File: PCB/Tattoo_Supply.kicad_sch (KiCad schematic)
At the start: 6 parts, among them J1 Barrel_Jack_Switch, J2 Out_{1}, J3 Out_{2}, Q1 SiA441DJ

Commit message: continue bom
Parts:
- J2, J3: footprint (none) -> TattooSupplyFootprints:MJ63022A
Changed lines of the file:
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@@
     (rev "V1.0")
   )
-  (bus_alias "USB2" (members "D+" "D-"))
-  (bus_alias "SPI" (members "~{CS}" "SCK" "MOSI" "MISO"))
-  (bus_alias "Encoder" (members "DT" "CLK" "SW"))
   (bus_alias "UART" (members "Tx" "Rx"))
   (bus_alias "I2C" (members "SDA" "SCL"))
+  (bus_alias "SPI" (members "~{CS}" "SCK" "MOSI" "MISO"))
+  (bus_alias "USB2" (members "D+" "D-"))
+  (bus_alias "Encoder" (members "DT" "CLK" "SW"))
   (junction (at 46.99 119.38) (diameter 0) (color 0 0 0 0)
   )
@@
       (effects (font (size 1.27 1.27)) (justify right))
     )
-    (property "Footprint" "" (at 251.46 43.18 0)
+    (property "Footprint" "TattooSupplyFootprints:MJ63022A" (at 251.46 43.18 0)
       (effects (font (size 1.27 1.27)) hide)
     )
@@
       (effects (font (size 1.27 1.27)) (justify right))
     )
-    (property "Footprint" "" (at 251.46 74.93 0)
-      (effects (font (size 1.27 1.27)) hide)
-    )
+    (property "Footprint" "TattooSupplyFootprints:MJ63022A" (at 251.46 74.93 0)
+      (effects (font (size 1.27 1.27)) hide)
+    )

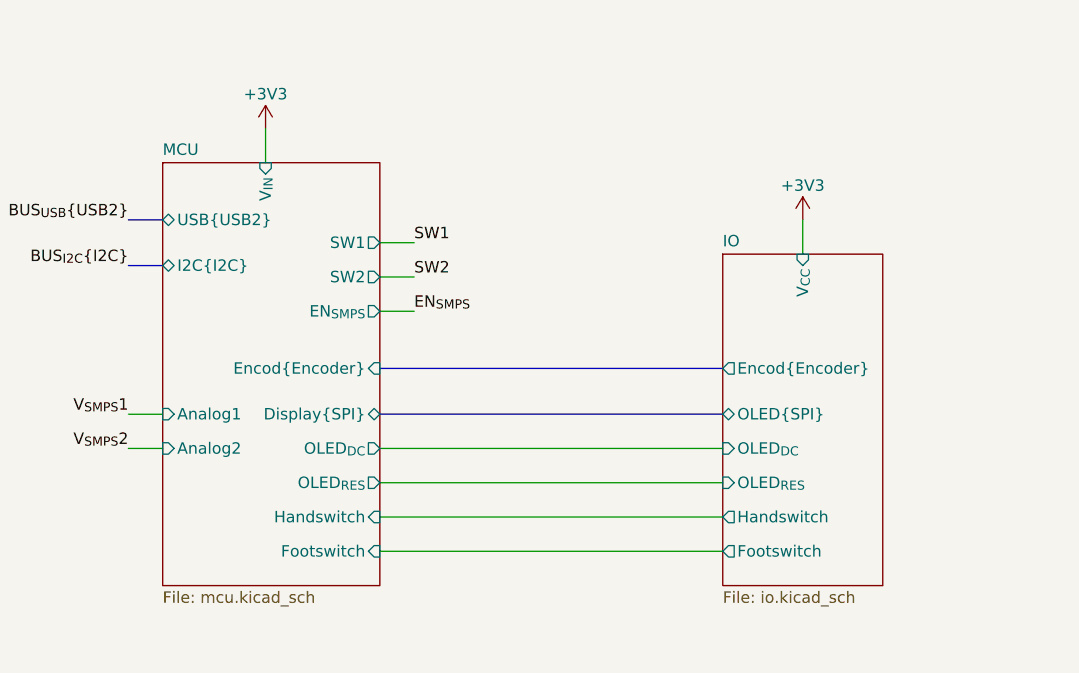
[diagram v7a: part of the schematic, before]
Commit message: schematic done and bom ok
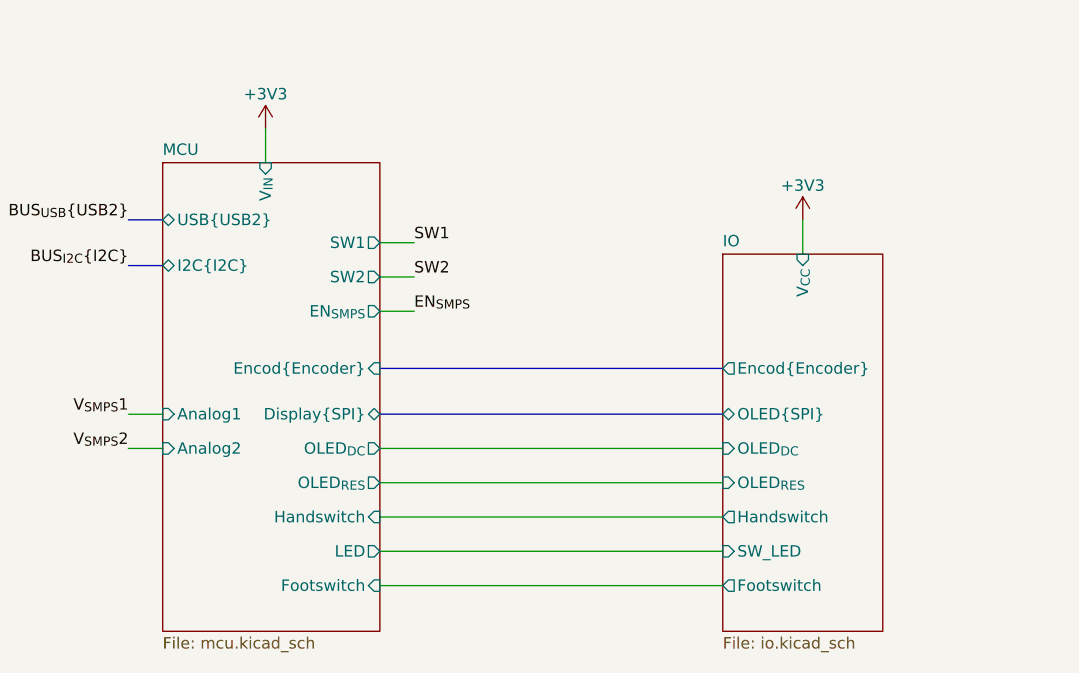
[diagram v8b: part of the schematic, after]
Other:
- sheet IO ports: added SW_LED; removed none
- sheet MCU ports: added LED; removed none
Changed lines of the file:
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@@
     (rev "V1.0")
   )
-  (bus_alias "UART" (members "Tx" "Rx"))
-  (bus_alias "I2C" (members "SDA" "SCL"))
   (bus_alias "SPI" (members "~{CS}" "SCK" "MOSI" "MISO"))
   (bus_alias "USB2" (members "D+" "D-"))
+  (bus_alias "I2C" (members "SDA" "SCL"))
+  (bus_alias "UART" (members "Tx" "Rx"))
   (bus_alias "Encoder" (members "DT" "CLK" "SW"))
   (junction (at 46.99 119.38) (diameter 0) (color 0 0 0 0)
@@
     (stroke (width 0) (type default))
   )
+  (wire (pts (xy 168.91 154.94) (xy 207.01 154.94))
+    (stroke (width 0) (type default))
+  )
   (wire (pts (xy 166.37 72.39) (xy 166.37 74.93))
     (stroke (width 0) (type default))
@@
     (stroke (width 0) (type default))
   )
-  (wire (pts (xy 168.91 154.94) (xy 207.01 154.94))
+  (wire (pts (xy 168.91 158.75) (xy 207.01 158.75))
     (stroke (width 0) (type default))
   )
@@
     )
   )
-  (sheet (at 207.01 121.92) (size 17.78 36.83) (fields_autoplaced)
+  (sheet (at 207.01 121.92) (size 17.78 41.91) (fields_autoplaced)
     (stroke (width 0.1524) (type solid))
     (fill (color 0 0 0 0.0000))
@@
       (effects (font (size 1.27 1.27)) (justify left bottom))
     )
-    (property "Sheetfile" "io.kicad_sch" (at 207.01 159.3346 0)
+    (property "Sheetfile" "io.kicad_sch" (at 207.01 164.4146 0)
       (effects (font (size 1.27 1.27)) (justify left top))
     )
@@
       (effects (font (size 1.27 1.27)) (justify right))
     )
-    (pin "Footswitch" output (at 207.01 154.94 180)
+    (pin "Footswitch" output (at 207.01 158.75 180)
       (effects (font (size 1.27 1.27)) (justify left))
     )
@@
     )
     (pin "OLED_{RES}" input (at 207.01 147.32 180)
+      (effects (font (size 1.27 1.27)) (justify left))
+    )
+    (pin "SW_LED" input (at 207.01 154.94 180)
       (effects (font (size 1.27 1.27)) (justify left))
     )
@@
     )
   )
-  (sheet (at 144.78 111.76) (size 24.13 46.99) (fields_autoplaced)
+  (sheet (at 144.78 111.76) (size 24.13 52.07) (fields_autoplaced)
     (stroke (width 0.1524) (type solid))
     (fill (color 0 0 0 0.0000))
@@
       (effects (font (size 1.27 1.27)) (justify left bottom))
     )
-    (property "Sheetfile" "mcu.kicad_sch" (at 144.78 159.3346 0)
+    (property "Sheetfile" "mcu.kicad_sch" (at 144.78 164.4146 0)
       (effects (font (size 1.27 1.27)) (justify left top))
     )
@@
       (effects (font (size 1.27 1.27)) (justify right))
     )
-    (pin "Footswitch" input (at 168.91 154.94 0)
+    (pin "Footswitch" input (at 168.91 158.75 0)
       (effects (font (size 1.27 1.27)) (justify right))
     )
@@
       (effects (font (size 1.27 1.27)) (justify right))
     )
+    (pin "LED" output (at 168.91 154.94 0)
+      (effects (font (size 1.27 1.27)) (justify right))
+    )
